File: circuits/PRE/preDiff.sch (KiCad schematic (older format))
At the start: 19 parts

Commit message: modificado el pre
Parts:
- added P1, P2, P3: CONN_1, symbol CONN_1
- added R11: 10K, symbol R
- gave numbers to parts that had none: 16
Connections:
- net labels added: GND
- wire segments 24 -> 30
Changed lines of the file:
@@
-EESchema Schematic File Version 2  date Fri 01 Apr 2016 11:37:16 AM ART
+EESchema Schematic File Version 2  date Fri 01 Apr 2016 11:49:08 AM ART
 LIBS:power
 LIBS:device
@@
 Comment4 ""
 $EndDescr
+Connection ~ 1700 4350
+Connection ~ 1700 3600
+Connection ~ 1700 2800
+$Comp
+L PWR_FLAG #FLG01
+U 1 1 56FE8A32
+P 5800 2600
+F 0 "#FLG01" H 5800 2695 30  0001 C CNN
+F 1 "PWR_FLAG" H 5800 2780 30  0000 C CNN
+	1    5800 2600
+	0    -1   -1   0
+$EndComp
+$Comp
+L PWR_FLAG #FLG02
+U 1 1 56FE8A22
+P 4300 2500
+F 0 "#FLG02" H 4300 2595 30  0001 C CNN
+F 1 "PWR_FLAG" H 4300 2680 30  0000 C CNN
+	1    4300 2500
+	0    -1   -1   0
+$EndComp
+$Comp
+L PWR_FLAG #FLG03
+U 1 1 56FE8A19
+P 1200 3600
+F 0 "#FLG03" H 1200 3695 30  0001 C CNN
+F 1 "PWR_FLAG" H 1200 3780 30  0000 C CNN
+	1    1200 3600
+	1    0    0    -1
+$EndComp
+$Comp
+L CONN_1 P2
+U 1 1 56FE8A10
+P 1350 4350
+F 0 "P2" H 1430 4350 40  0000 L CNN
+F 1 "CONN_1" H 1350 4405 30  0001 C CNN
+	1    1350 4350
+	-1   0    0    1
+$EndComp
+$Comp
+L CONN_1 P1
+U 1 1 56FE8A08
+P 1350 2800
+F 0 "P1" H 1430 2800 40  0000 L CNN
+F 1 "CONN_1" H 1350 2855 30  0001 C CNN
+	1    1350 2800
+	-1   0    0    1
+$EndComp
+$Comp
+L CONN_1 P3
+U 1 1 56FE8A00
+P 7000 3000
+F 0 "P3" H 7080 3000 40  0000 L CNN
+F 1 "CONN_1" H 7000 3055 30  0001 C CNN
+	1    7000 3000
+	1    0    0    -1
+$EndComp
+$Comp
+L GND #PWR04
+U 1 1 56FE89F6
+P 1200 3750
+F 0 "#PWR04" H 1200 3750 30  0001 C CNN
+F 1 "GND" H 1200 3680 30  0001 C CNN
+	1    1200 3750
+	1    0    0    -1
+$EndComp
+Wire Wire Line
+	1200 3600 1200 3750
+Wire Wire Line
+	6400 2250 6400 3000
+Wire Wire Line
+	6400 2250 6050 2250
 Connection ~ 2700 4350
 Wire Wire Line
@@
 	2700 2800 2700 3350
 Connection ~ 2700 2800
-$Comp
-L TL074 U?
-U 1 1 56FE7262
+Wire Wire Line
+	5550 2250 5400 2250
+Wire Wire Line
+	5400 2250 5400 2900
+Wire Wire Line
+	6400 4350 6400 4450
+Connection ~ 6400 3000
+$Comp
+L GND #PWR05
+U 1 1 56FE89D1
+P 6400 4450
+F 0 "#PWR05" H 6400 4450 30  0001 C CNN
+F 1 "GND" H 6400 4380 30  0001 C CNN
+	1    6400 4450
+	1    0    0    -1
+$EndComp
+$Comp
+L R R11
+U 1 1 56FE8981
+P 5800 2250
+F 0 "R11" V 5880 2250 50  0000 C CNN
+F 1 "10K" V 5800 2250 50  0000 C CNN
+	1    5800 2250
+	0    -1   -1   0
+$EndComp
+$Comp
+L TL074 U1
+U 4 1 56FE7262
 P 5900 4250
-F 0 "U?" H 5950 4450 60  0000 C CNN
+F 0 "U1" H 5950 4450 60  0000 C CNN
 F 1 "TL074" H 6050 4050 50  0000 C CNN
-	1    5900 4250
-	-1   0    0    1
-$EndComp
-$Comp
-L TL074 U?
-U 1 1 56FE725F
+	4    5900 4250
+	-1   0    0    1
+$EndComp
+$Comp
+L TL074 U1
+U 3 1 56FE725F
 P 5900 3000
-F 0 "U?" H 5950 3200 60  0000 C CNN
+F 0 "U1" H 5950 3200 60  0000 C CNN
 F 1 "TL074" H 6050 2800 50  0000 C CNN
-	1    5900 3000
+	3    5900 3000
 	1    0    0    1
 $EndComp
 $Comp
-L TL074 U?
-U 1 1 56FE725B
+L TL074 U1
+U 2 1 56FE725B
 P 4400 4250
-F 0 "U?" H 4450 4450 60  0000 C CNN
+F 0 "U1" H 4450 4450 60  0000 C CNN
 F 1 "TL074" H 4550 4050 50  0000 C CNN
-	1    4400 4250
+	2    4400 4250
 	1    0    0    1
 $EndComp
 $Comp
-L TL074 U?
+L TL074 U1
 U 1 1 56FE7221
 P 4400 2900
-F 0 "U?" H 4450 3100 60  0000 C CNN
+F 0 "U1" H 4450 3100 60  0000 C CNN
 F 1 "TL074" H 4550 2700 50  0000 C CNN
 	1    4400 2900
@@
 $EndComp
 $Comp
-L VDD #PWR?
+L VDD #PWR06
 U 1 1 56FE7200
 P 5800 2600
-F 0 "#PWR?" H 5800 2700 30  0001 C CNN
+F 0 "#PWR06" H 5800 2700 30  0001 C CNN
 F 1 "VDD" H 5800 2710 30  0000 C CNN
 	1    5800 2600
@@
 $EndComp
 $Comp
-L VCC #PWR?
+L VCC #PWR07
 U 1 1 56FE70C7
 P 4300 2500
-F 0 "#PWR?" H 4300 2600 30  0001 C CNN
+F 0 "#PWR07" H 4300 2600 30  0001 C CNN
 F 1 "VCC" H 4300 2600 30  0000 C CNN
 	1    4300 2500
@@
 $EndComp
 $Comp
-L R R?
+L R R5
 U 1 1 56FD6067
 P 2450 4350
-F 0 "R?" V 2530 4350 50  0000 C CNN
+F 0 "R5" V 2530 4350 50  0000 C CNN
 F 1 "R" V 2450 4350 50  0000 C CNN
 	1    2450 4350
@@
 $EndComp
 $Comp
-L R R?
+L R R4
 U 1 1 56FD6061
 P 2450 2800
-F 0 "R?" V 2530 2800 50  0000 C CNN
+F 0 "R4" V 2530 2800 50  0000 C CNN
 F 1 "R" V 2450 2800 50  0000 C CNN
 	1    2450 2800
@@
 $EndComp
 $Comp
-L R R?
+L R R1
 U 1 1 56FD5FEC
 P 1450 3600
-F 0 "R?" V 1530 3600 50  0000 C CNN
+F 0 "R1" V 1530 3600 50  0000 C CNN
 F 1 "R" V 1450 3600 50  0000 C CNN
 	1    1450 3600
@@
 $EndComp
 $Comp
-L R R?
+L R R3
 U 1 1 56FD5FE4
 P 1700 4100
-F 0 "R?" V 1780 4100 50  0000 C CNN
+F 0 "R3" V 1780 4100 50  0000 C CNN
 F 1 "R" V 1700 4100 50  0000 C CNN
 	1    1700 4100
@@
 $EndComp
 $Comp
-L R R?
+L R R2
 U 1 1 56FD5FD8
 P 1700 3050
-F 0 "R?" V 1780 3050 50  0000 C CNN
+F 0 "R2" V 1780 3050 50  0000 C CNN
 F 1 "R" V 1700 3050 50  0000 C CNN
 	1    1700 3050
@@
 $EndComp
 $Comp
-L C C?
+L C C1
 U 1 1 56FD5FC2
 P 2700 3550
-F 0 "C?" H 2750 3650 50  0000 L CNN
+F 0 "C1" H 2750 3650 50  0000 L CNN
 F 1 "C" H 2750 3450 50  0000 L CNN
 	1    2700 3550
@@
 $EndComp
 $Comp
-L POT RV?
+L POT RV1
 U 1 1 56FD5F90
 P 3650 3450
-F 0 "RV?" H 3650 3350 50  0000 C CNN
+F 0 "RV1" H 3650 3350 50  0000 C CNN
 F 1 "POT" H 3650 3450 50  0000 C CNN
 	1    3650 3450
@@
 $EndComp
 $Comp
-L R R?
+L R R6
 U 1 1 56FD5F7F
 P 3250 3700
-F 0 "R?" V 3330 3700 50  0000 C CNN
+F 0 "R6" V 3330 3700 50  0000 C CNN
 F 1 "R" V 3250 3700 50  0000 C CNN
 	1    3250 3700
@@
 $EndComp
 $Comp
-L C C?
+L C C3
 U 1 1 56FD5F65
 P 5900 3700
-F 0 "C?" H 5950 3800 50  0000 L CNN
+F 0 "C3" H 5950 3800 50  0000 L CNN
 F 1 "C" H 5950 3600 50  0000 L CNN
 	1    5900 3700
@@
 $EndComp
 $Comp
-L CP C?
+L CP C2
 U 1 1 56FD5F43
 P 3700 3700
-F 0 "C?" H 3750 3800 50  0000 L CNN
+F 0 "C2" H 3750 3800 50  0000 L CNN
 F 1 "CP" H 3750 3600 50  0000 L CNN
 	1    3700 3700
@@
 $EndComp
 $Comp
-L R R?
+L R R7
 U 1 1 56FD5EF5
 P 4300 3450
-F 0 "R?" V 4380 3450 50  0000 C CNN
+F 0 "R7" V 4380 3450 50  0000 C CNN
 F 1 "R" V 4300 3450 50  0000 C CNN
 	1    4300 3450
@@
 $EndComp
 $Comp
-L R R?
+L R R8
 U 1 1 56FD5EEB
 P 4300 3700
-F 0 "R?" V 4380 3700 50  0000 C CNN
+F 0 "R8" V 4380 3700 50  0000 C CNN
 F 1 "R" V 4300 3700 50  0000 C CNN
 	1    4300 3700
@@
 $EndComp
 $Comp
-L R R?
+L R R12
 U 1 1 56FD5D1B
 P 6400 3250
-F 0 "R?" V 6480 3250 50  0000 C CNN
+F 0 "R12" V 6480 3250 50  0000 C CNN
 F 1 "R" V 6400 3250 50  0000 C CNN
 	1    6400 3250
@@
 $EndComp
 $Comp
-L R R?
+L R R10
 U 1 1 56FD5CB0
 P 5150 4250
-F 0 "R?" V 5230 4250 50  0000 C CNN
+F 0 "R10" V 5230 4250 50  0000 C CNN
 F 1 "R" V 5150 4250 50  0000 C CNN
 	1    5150 4250
@@
 $EndComp
 $Comp
-L R R?
+L R R9
 U 1 1 56FD5CA8
 P 5150 2900
-F 0 "R?" V 5230 2900 50  0000 C CNN
+F 0 "R9" V 5230 2900 50  0000 C CNN
 F 1 "R" V 5150 2900 50  0000 C CNN
 	1    5150 2900

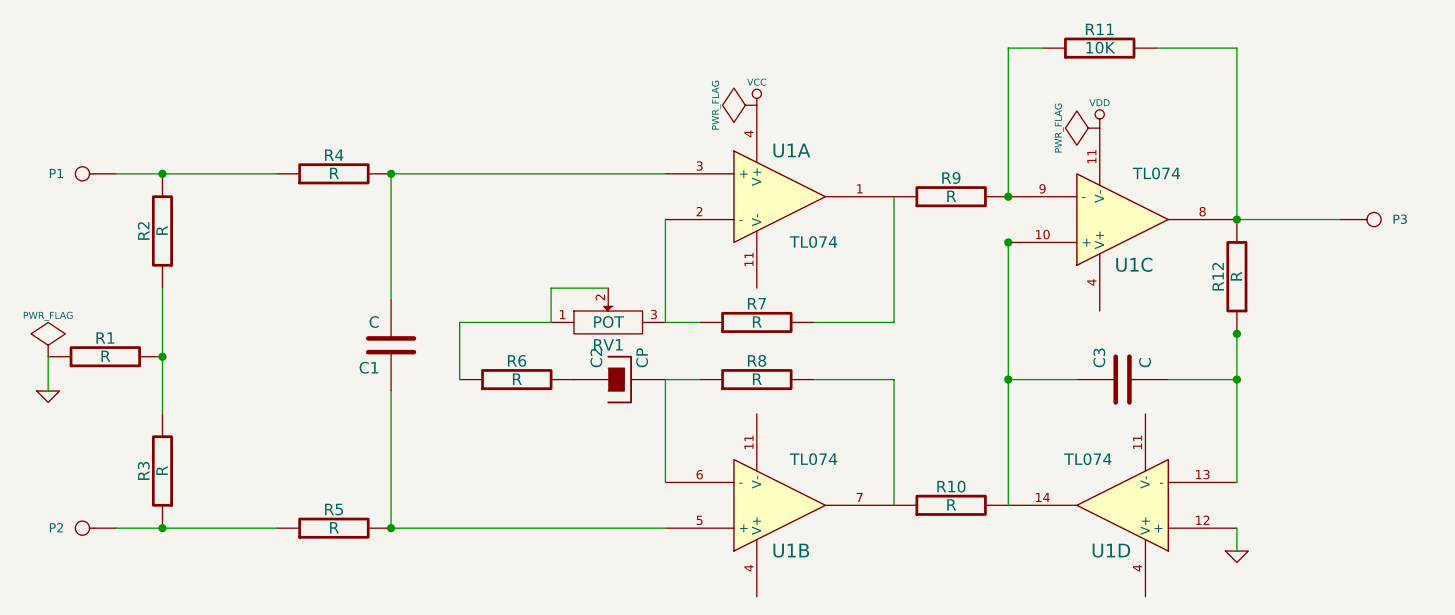
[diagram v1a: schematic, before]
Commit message: resistencia de realimentacion agregada
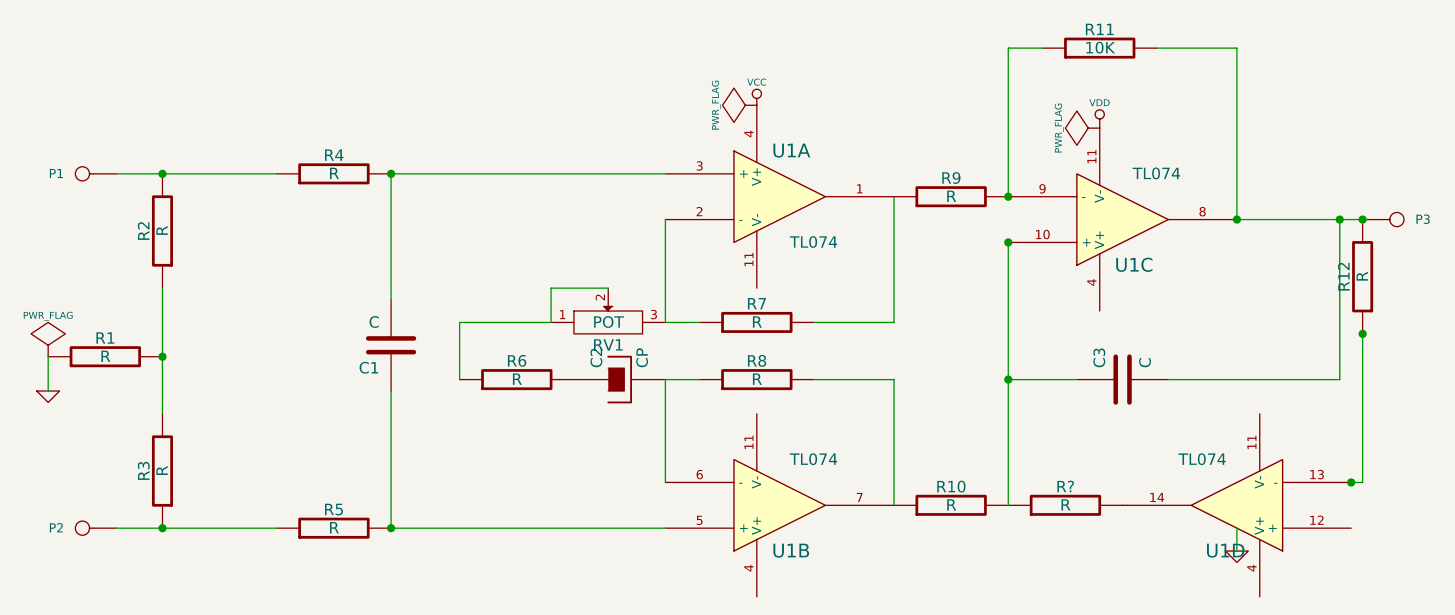
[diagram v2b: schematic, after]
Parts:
- added R?: R, symbol R
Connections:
- net GND: no longer U1.12 (+)
- net at C3.1, R10.2, U1.10 (+): now also R?.1; no longer U1.14
- net at R12.1, U1.13 (-): no longer C3.2
- net at P3.1, R11.2, R12.2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: now also C3.2
- new net: R?.2, U1.14
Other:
- moved on the sheet: P3, R12, U1D
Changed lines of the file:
@@
-EESchema Schematic File Version 2  date Fri 01 Apr 2016 11:49:08 AM ART
+EESchema Schematic File Version 2  date Fri 01 Apr 2016 11:59:19 AM ART
 LIBS:power
 LIBS:device
@@
 Comment4 ""
 $EndDescr
+Connection ~ 6900 4150
+Connection ~ 6950 3500
+Connection ~ 6950 3000
+Connection ~ 6850 3000
+Wire Wire Line
+	6950 3000 6400 3000
+Wire Wire Line
+	6850 3000 6850 3700
+Wire Wire Line
+	6850 3700 6100 3700
+Connection ~ 6400 3000
+Wire Wire Line
+	6400 4350 6400 4450
+Wire Wire Line
+	5400 2900 5400 2250
+Wire Wire Line
+	5400 2250 5550 2250
+Connection ~ 2700 2800
+Wire Wire Line
+	2700 3350 2700 2800
+Wire Wire Line
+	3900 4350 2700 4350
+Wire Wire Line
+	2200 4350 1500 4350
+Wire Wire Line
+	3400 3300 3400 3450
+Wire Wire Line
+	3400 3300 3650 3300
+Wire Wire Line
+	4900 4250 4900 3700
+Wire Wire Line
+	4900 3700 4550 3700
+Wire Wire Line
+	3900 3000 3900 3450
+Wire Wire Line
+	3900 3450 4050 3450
+Connection ~ 5400 3700
+Connection ~ 5400 2900
+Connection ~ 5400 3100
+Wire Wire Line
+	5400 3100 5400 4250
+Wire Wire Line
+	5700 3700 5400 3700
+Wire Wire Line
+	4550 3450 4900 3450
+Wire Wire Line
+	4900 3450 4900 2900
+Wire Wire Line
+	4050 3700 3900 3700
+Wire Wire Line
+	3900 3700 3900 4150
+Wire Wire Line
+	3400 3450 3000 3450
+Wire Wire Line
+	3000 3450 3000 3700
+Wire Wire Line
+	1500 2800 2200 2800
+Wire Wire Line
+	2700 2800 3900 2800
+Wire Wire Line
+	1700 3850 1700 3300
+Wire Wire Line
+	2700 4350 2700 3750
+Connection ~ 2700 4350
+Wire Wire Line
+	6050 2250 6400 2250
+Wire Wire Line
+	6400 2250 6400 3000
+Wire Wire Line
+	1200 3600 1200 3750
+Connection ~ 1700 2800
+Connection ~ 1700 3600
 Connection ~ 1700 4350
-Connection ~ 1700 3600
-Connection ~ 1700 2800
+Wire Wire Line
+	6900 4150 6950 4150
+Wire Wire Line
+	6950 4150 6950 3500
+$Comp
+L R R?
+U 1 1 56FE8C82
+P 5650 4250
+F 0 "R?" V 5730 4250 50  0000 C CNN
+F 1 "R" V 5650 4250 50  0000 C CNN
+	1    5650 4250
+	0    -1   -1   0
+$EndComp
 $Comp
 L PWR_FLAG #FLG01
@@
 L CONN_1 P3
 U 1 1 56FE8A00
-P 7000 3000
-F 0 "P3" H 7080 3000 40  0000 L CNN
-F 1 "CONN_1" H 7000 3055 30  0001 C CNN
-	1    7000 3000
+P 7100 3000
+F 0 "P3" H 7180 3000 40  0000 L CNN
+F 1 "CONN_1" H 7100 3055 30  0001 C CNN
+	1    7100 3000
 	1    0    0    -1
 $EndComp
@@
 	1    0    0    -1
 $EndComp
-Wire Wire Line
-	1200 3600 1200 3750
-Wire Wire Line
-	6400 2250 6400 3000
-Wire Wire Line
-	6400 2250 6050 2250
-Connection ~ 2700 4350
-Wire Wire Line
-	2700 3750 2700 4350
-Wire Wire Line
-	1700 3300 1700 3850
-Wire Wire Line
-	3900 2800 2700 2800
-Wire Wire Line
-	2200 2800 1500 2800
-Wire Wire Line
-	3000 3700 3000 3450
-Wire Wire Line
-	3000 3450 3400 3450
-Wire Wire Line
-	3900 4150 3900 3700
-Wire Wire Line
-	3900 3700 4050 3700
-Wire Wire Line
-	4900 2900 4900 3450
-Wire Wire Line
-	4900 3450 4550 3450
-Wire Wire Line
-	5700 3700 5400 3700
-Wire Wire Line
-	6400 4150 6400 3500
-Wire Wire Line
-	5400 4250 5400 3100
-Connection ~ 6400 3500
-Connection ~ 5400 3100
-Connection ~ 5400 2900
-Connection ~ 5400 3700
-Wire Wire Line
-	6100 3700 6400 3700
-Connection ~ 6400 3700
-Wire Wire Line
-	6400 3000 6850 3000
-Wire Wire Line
-	4050 3450 3900 3450
-Wire Wire Line
-	3900 3450 3900 3000
-Wire Wire Line
-	4550 3700 4900 3700
-Wire Wire Line
-	4900 3700 4900 4250
-Wire Wire Line
-	3650 3300 3400 3300
-Wire Wire Line
-	3400 3300 3400 3450
-Wire Wire Line
-	1500 4350 2200 4350
-Wire Wire Line
-	2700 4350 3900 4350
-Wire Wire Line
-	2700 2800 2700 3350
-Connection ~ 2700 2800
-Wire Wire Line
-	5550 2250 5400 2250
-Wire Wire Line
-	5400 2250 5400 2900
-Wire Wire Line
-	6400 4350 6400 4450
-Connection ~ 6400 3000
 $Comp
 L GND #PWR05
@@
 L TL074 U1
 U 4 1 56FE7262
-P 5900 4250
-F 0 "U1" H 5950 4450 60  0000 C CNN
-F 1 "TL074" H 6050 4050 50  0000 C CNN
-	4    5900 4250
+P 6400 4250
+F 0 "U1" H 6450 4450 60  0000 C CNN
+F 1 "TL074" H 6550 4050 50  0000 C CNN
+	4    6400 4250
 	-1   0    0    1
 $EndComp
@@
 L R R12
 U 1 1 56FD5D1B
-P 6400 3250
-F 0 "R12" V 6480 3250 50  0000 C CNN
-F 1 "R" V 6400 3250 50  0000 C CNN
-	1    6400 3250
-	-1   0    0    1
-$EndComp
+P 6950 3250
+F 0 "R12" V 7030 3250 50  0000 C CNN
+F 1 "R" V 6950 3250 50  0000 C CNN
+	1    6950 3250
+	-1   0    0    1
+$EndComp

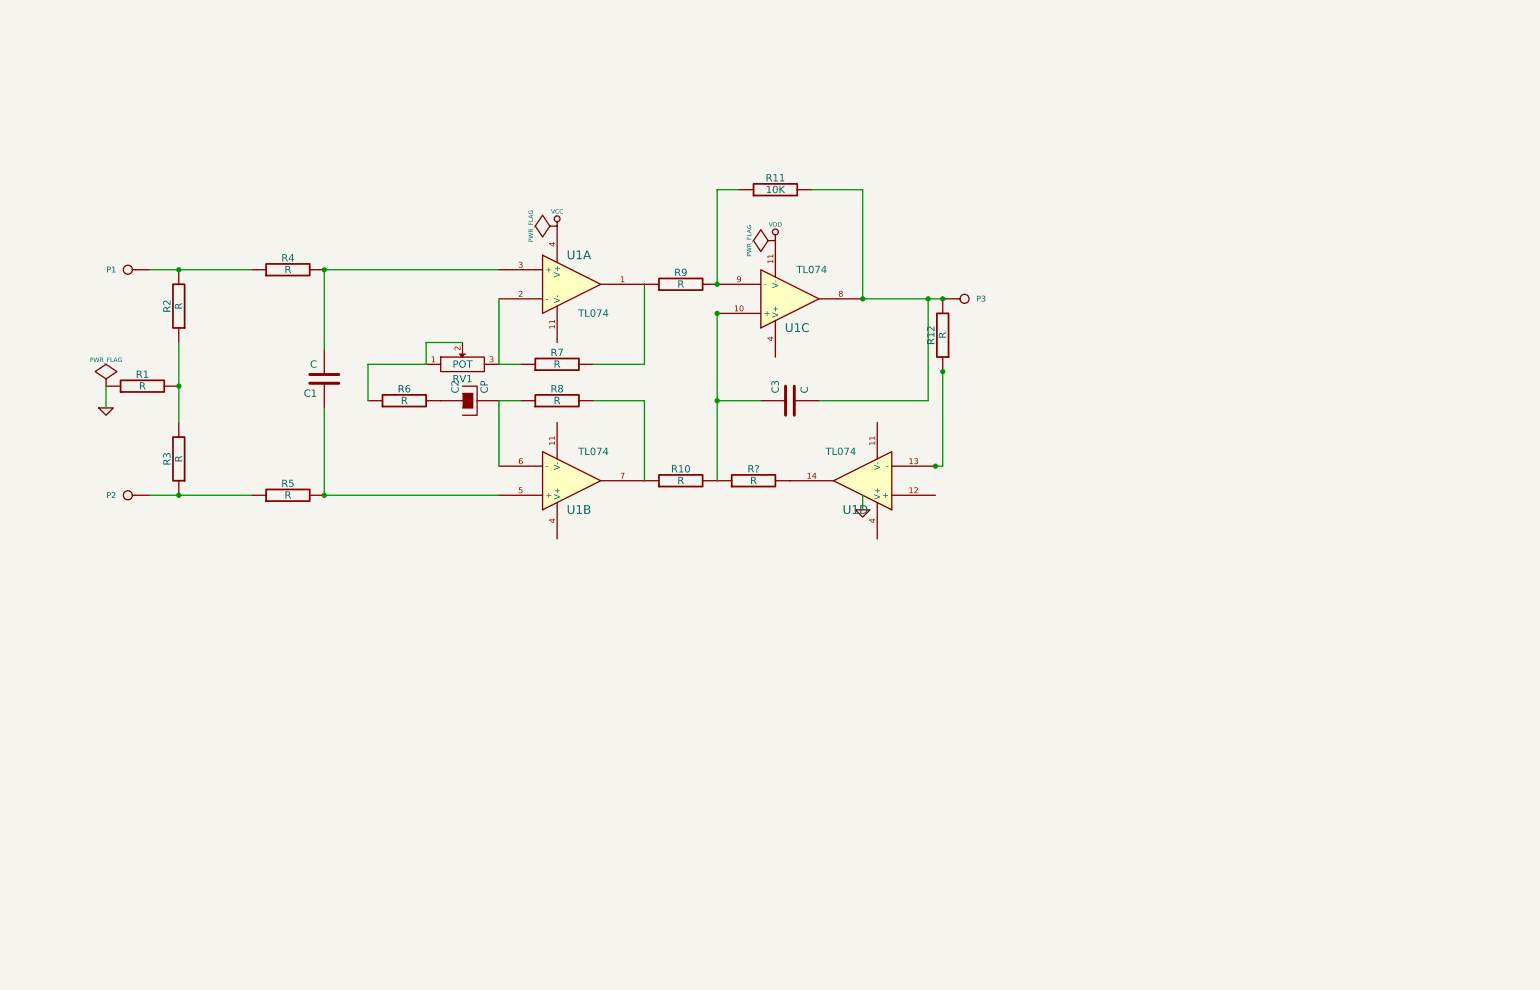
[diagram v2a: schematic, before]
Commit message: ampli diff completo
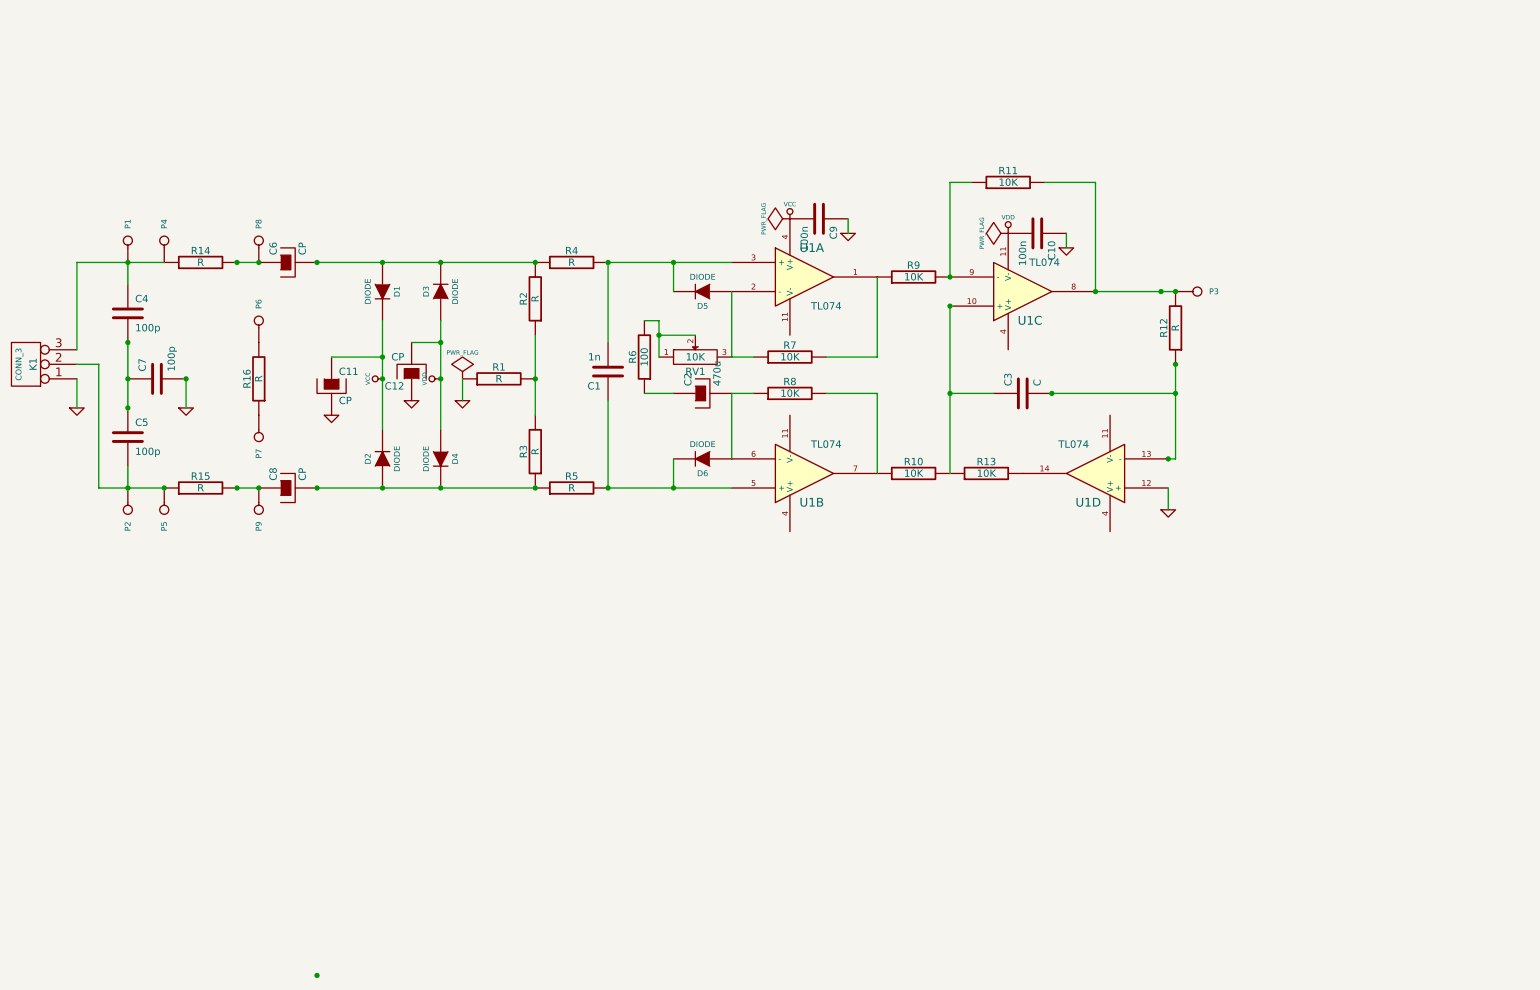
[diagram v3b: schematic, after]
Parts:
- added C10, C9: 100n, symbol C
- added C11, C12, C6, C8: CP, symbol CP
- added C4, C5, C7: 100p, symbol C
- added D1, D2, D3, D4, D5, D6: DIODE, symbol DIODE
- added K1: CONN_3, symbol CONN_3
- added P4, P5, P6, P7, P8, P9: CONN_1, symbol CONN_1
- added R14, R15, R16: R, symbol R
- C1: value C -> 1n
- C2: value CP -> 470u
- R10, R7, R8, R9: value R -> 10K
- R13: renamed from R?; value R -> 10K
- R6: value R -> 100
- RV1: value POT -> 10K
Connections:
- net GND: now also U1.12 (+), C10.1, C11.2, C12.1, C7.2, C9.1, K1.1 (P1)
- net VCC: now also C11.1, C9.2, D1.2 (K), D2.2 (K)
- net VDD: now also C10.2, C12.2, D3.1 (A), D4.1 (A)
- net at R12.1, U1.13 (-): now also C3.2
- net at P3.1, R11.2, R12.2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: no longer C3.2
- net at C2.2, R8.1, U1.6 (-): now also D6.1 (A)
- net at R7.1, RV1.3, U1.2 (-): now also D5.1 (A)
- net at C2.1: now also R6.1; no longer R6.2
- net at RV1.1, RV1.2: now also R6.2; no longer R6.1
- net at C1.1, R5.2, U1.5 (+): now also D6.2 (K)
- net at C1.2, R4.2, U1.3 (+): now also D5.2 (K)
- net at R2.2, R4.1: now also C6.2, D1.1 (A), D3.2 (K); no longer P1.1
- net at R3.1, R5.1: now also C8.2, D2.1 (A), D4.2 (K); no longer P2.1
- new net: C5.2, K1.2 (PM), P2.1, P5.1, R15.1
- new net: C4.1, K1.3 (P3), P1.1, P4.1, R14.1
- new net: C4.2, C5.1, C7.1
- new net: C6.1, P8.1, R14.2
- new net: C8.1, P9.1, R15.2
- new net: P7.1, R16.1
- new net: P6.1, R16.2
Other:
- moved on the sheet: C1, C2, C3, P3, R1, R10, R11, R12, R13, R2, R3, R4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
